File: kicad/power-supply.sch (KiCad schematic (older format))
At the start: 37 parts, among them Q4 BUK98180-100A, T1 BC846B, T10 BC846B, T2 BC846B, T3 BC846B, T4 BC856B, U4 LMR16006X

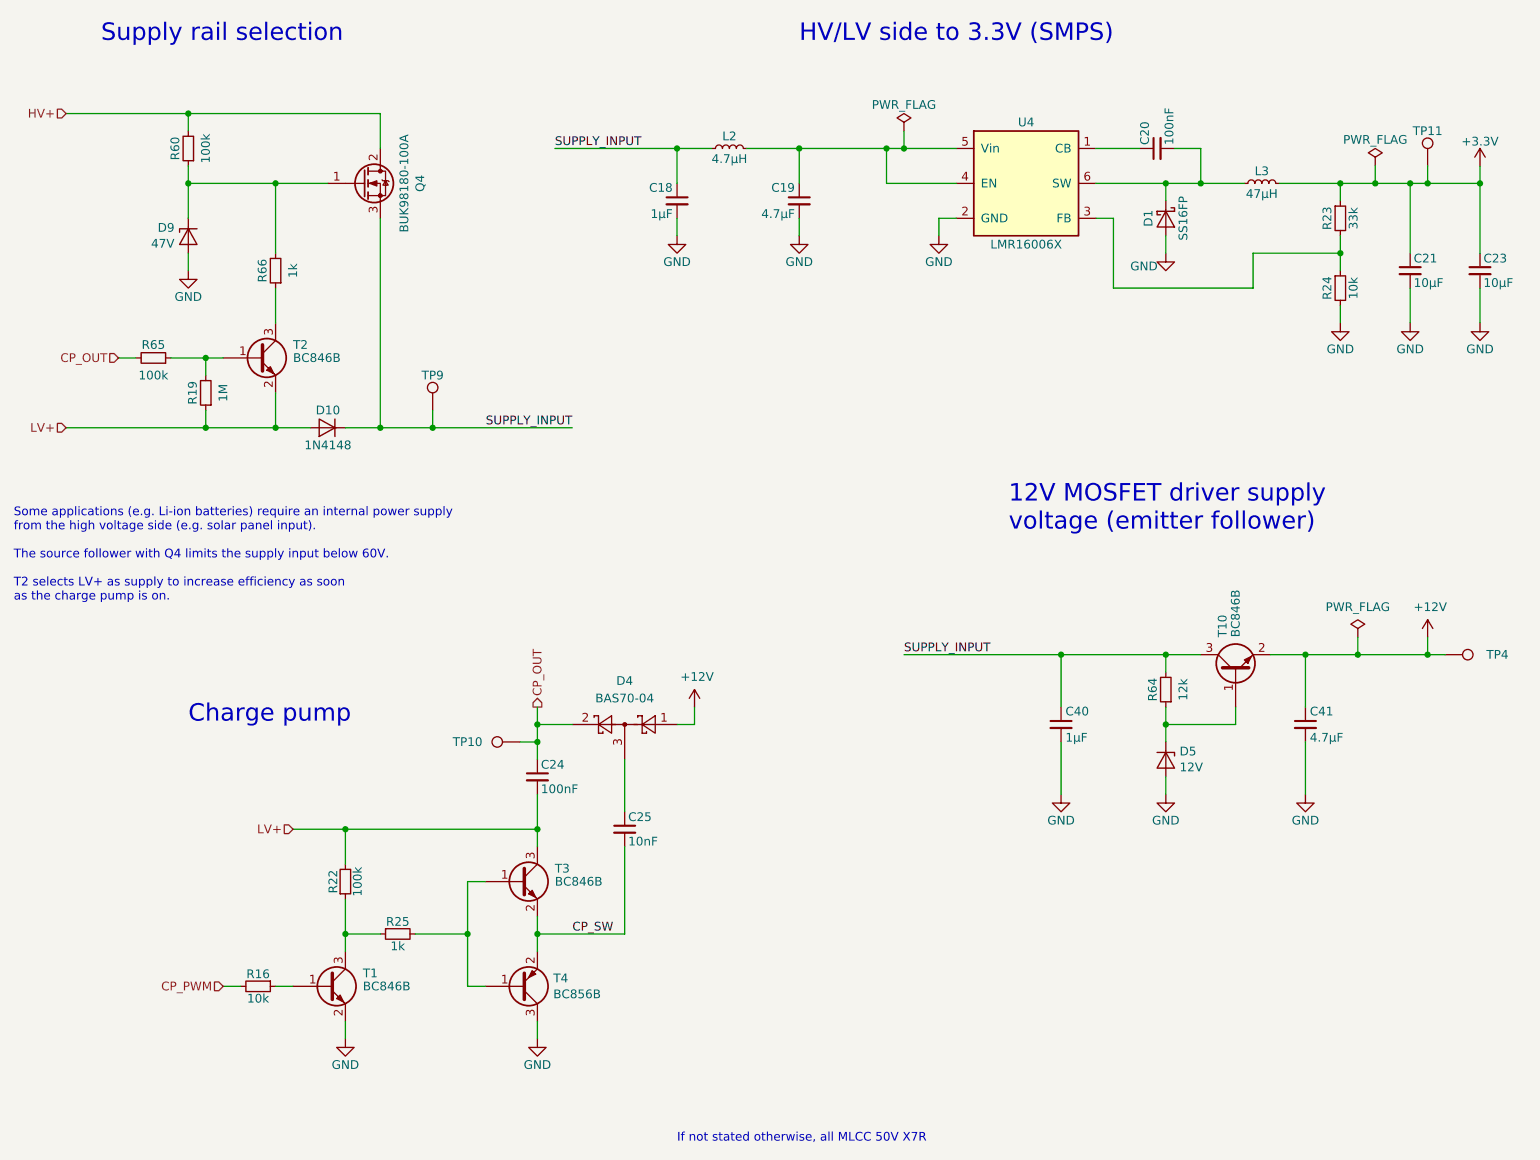
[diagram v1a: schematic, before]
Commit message: Update to v0.2 with improvements after testing
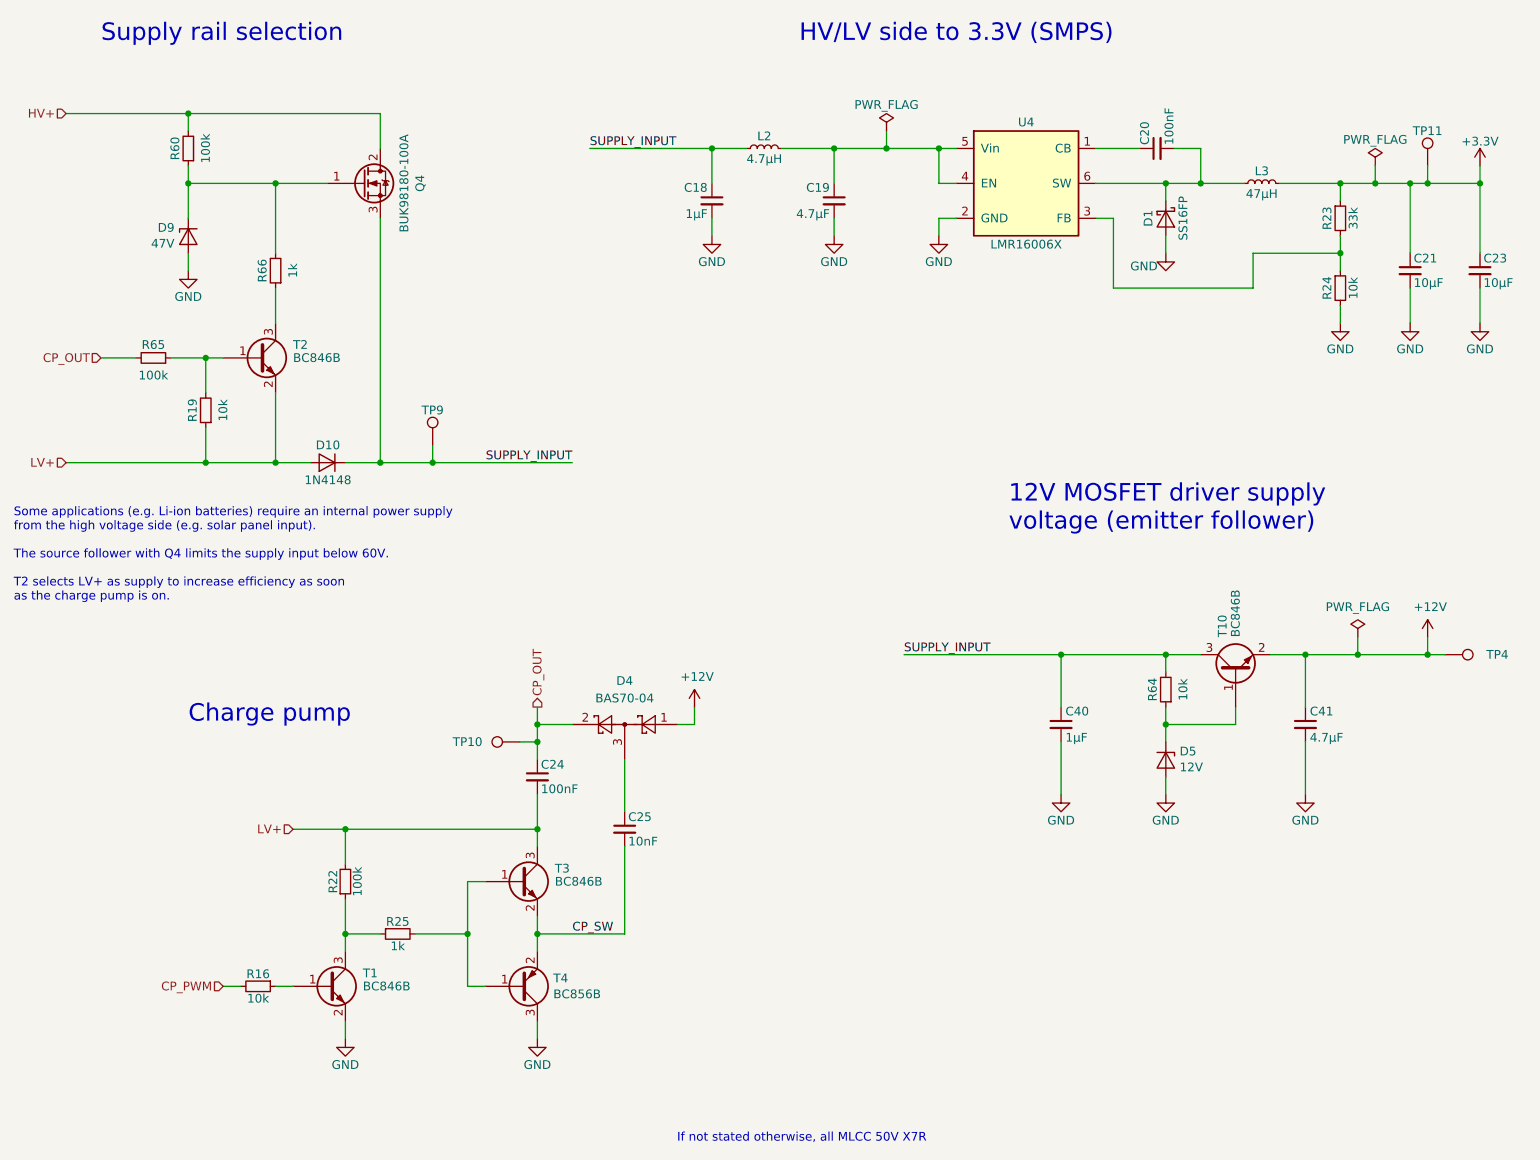
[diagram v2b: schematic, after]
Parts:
- D1: Remarks Alternativ: DFLS160-7 -> Alternative: DFLS160-7
- R19: value 1M -> 10k
- R64: value 12k -> 10k
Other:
- moved on the sheet: C18, C19, D10, L2, R19, TP9
